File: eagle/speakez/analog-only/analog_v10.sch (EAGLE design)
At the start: 51 parts, among them U1 +12v, U2 MAX5486

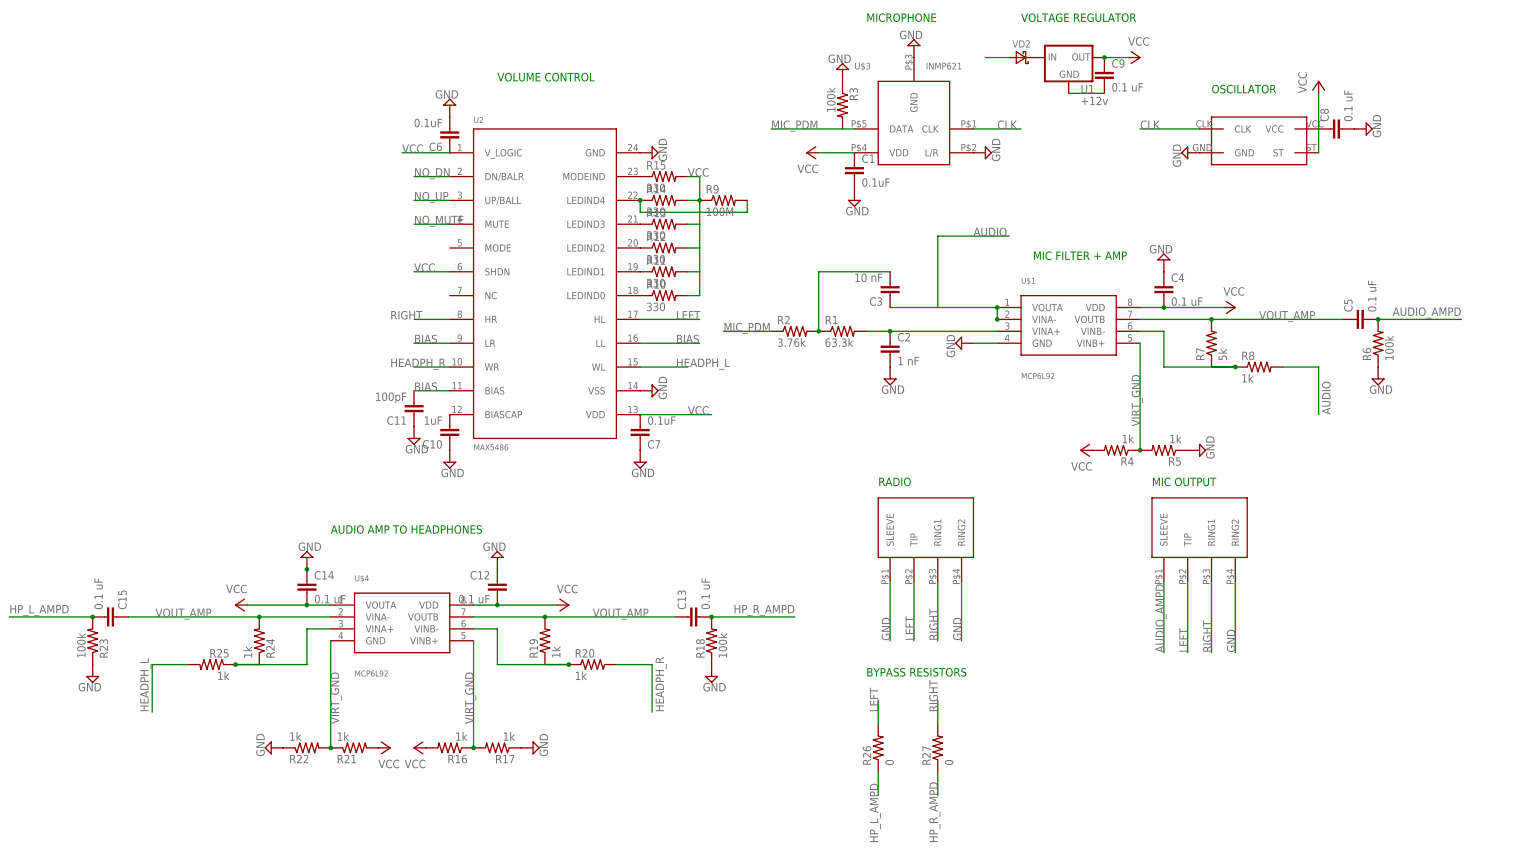
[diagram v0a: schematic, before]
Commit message: update L/R buffering, offsets, naming conventions, move info from nets layer to info layer
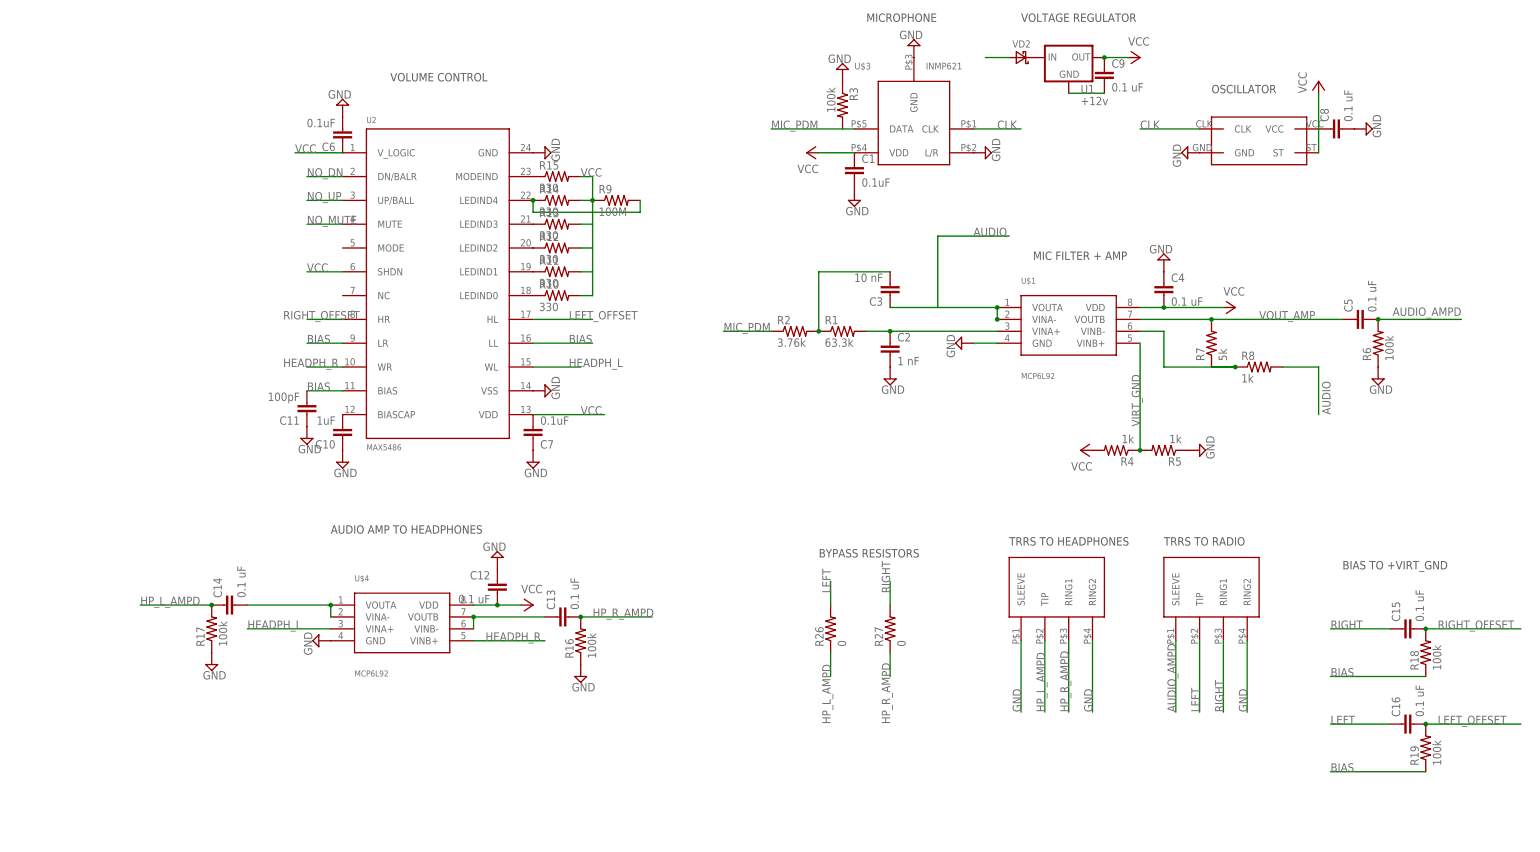
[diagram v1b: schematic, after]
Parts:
- removed R20, R24, R25: 1k, SparkFun-Resistors:RESISTOR0805-RES
- removed R21, R22: 1k, SparkFun-Passives:RESISTOR0805-RES
- removed R23: 100k, SparkFun-Resistors:RESISTOR0805-RES
- added C16: 0.1 uF, SparkFun-Passives:CAP0805
- R16, R17: value 1k -> 100k; device SparkFun-Passives:RESISTOR0805-RES -> SparkFun-Resistors:RESISTOR0805-RES
- R19: value 1k -> 100k
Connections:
- new net LEFT_OFFSET: C16.2, R19.2, U2.HL
- new net RIGHT_OFFSET: C15.2, R18.2, U2.HR
- net BIAS: now also R18.1, R19.1
- net GND: now also R16.1, U$4.GND; no longer C14.1, R18.1, R22.1, R23.1
- net HEADPH_L: now also U$4.VINA+; no longer R25.2
- net HEADPH_R: now also U$4.VINB+; no longer R20.2
- net HP_L_AMPD: now also C14.1, HP.TIP, R17.2; no longer C15.2, R23.2
- net HP_R_AMPD: now also HP.RING1, R16.2; no longer R18.2
- net LEFT: now also C16.1; no longer HP.TIP, U2.HL
- net N$10: now also C13.1, U$4.VOUTB; no longer R19.1, R20.1
- net N$14: now also C14.2, U$4.VINA-, U$4.VOUTA; no longer R24.1, R25.1, U$4.VINA+
- net RIGHT: now also C15.1; no longer HP.RING1, U2.HR
- net VCC: no longer C14.2, R16.2, R21.2, U$4.VOUTA
- net VIRT_GND: no longer R16.1, R17.2, R21.1, R22.2, U$4.GND, U$4.VINB+
- net VOUT_AMP: no longer C13.1, C15.1, R19.2, R24.2, U$4.VINA-, U$4.VOUTB
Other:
- note added: "BIAS TO +VIRT_GND"
- note added: "TRRS TO HEADPHONES"
- note added: "TRRS TO RADIO"
- note removed: "MIC OUTPUT"
- note removed: "RADIO"
- moved on the sheet: C10, C11, C13, C14, C15, C6, C7, R10, R11, R12, R13, R14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

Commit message: routed some of board
but doubting my routing
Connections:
- net GND renamed HEADPHONES_R
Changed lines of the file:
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@@
 <?xml version="1.0" encoding="utf-8"?>
 <!DOCTYPE eagle SYSTEM "eagle.dtd">
-<eagle version="7.6.0">
+<eagle version="7.7.0">
 <drawing>
 <settings>
@@
 <grid distance="0.1" unitdist="inch" unit="inch" style="lines" multiple="1" display="no" altdistance="0.01" altunitdist="inch" altunit="inch"/>
 <layers>
-<layer number="1" name="Top" color="4" fill="1" visible="no" active="no"/>
-<layer number="16" name="Bottom" color="1" fill="1" visible="no" active="no"/>
-<layer number="17" name="Pads" color="2" fill="1" visible="no" active="no"/>
-<layer number="18" name="Vias" color="2" fill="1" visible="no" active="no"/>
-<layer number="19" name="Unrouted" color="6" fill="1" visible="no" active="no"/>
-<layer number="20" name="Dimension" color="15" fill="1" visible="no" active="no"/>
-<layer number="21" name="tPlace" color="8" fill="1" visible="no" active="no"/>
-<layer number="22" name="bPlace" color="7" fill="1" visible="no" active="no"/>
-<layer number="23" name="tOrigins" color="15" fill="1" visible="no" active="no"/>
-<layer number="24" name="bOrigins" color="15" fill="1" visible="no" active="no"/>
-<layer number="25" name="tNames" color="8" fill="1" visible="no" active="no"/>
-<layer number="26" name="bNames" color="7" fill="1" visible="no" active="no"/>
-<layer number="27" name="tValues" color="8" fill="1" visible="no" active="no"/>
-<layer number="28" name="bValues" color="7" fill="1" visible="no" active="no"/>
+<layer number="1" name="Top" color="4" fill="1" visible="yes" active="no"/>
+<layer number="16" name="Bottom" color="1" fill="1" visible="yes" active="no"/>
+<layer number="17" name="Pads" color="2" fill="1" visible="yes" active="no"/>
+<layer number="18" name="Vias" color="2" fill="1" visible="yes" active="no"/>
+<layer number="19" name="Unrouted" color="6" fill="1" visible="yes" active="no"/>
+<layer number="20" name="Dimension" color="15" fill="1" visible="yes" active="no"/>
+<layer number="21" name="tPlace" color="8" fill="1" visible="yes" active="no"/>
+<layer number="22" name="bPlace" color="7" fill="1" visible="yes" active="no"/>
+<layer number="23" name="tOrigins" color="15" fill="1" visible="yes" active="no"/>
+<layer number="24" name="bOrigins" color="15" fill="1" visible="yes" active="no"/>
+<layer number="25" name="tNames" color="8" fill="1" visible="yes" active="no"/>
+<layer number="26" name="bNames" color="7" fill="1" visible="yes" active="no"/>
+<layer number="27" name="tValues" color="8" fill="1" visible="yes" active="no"/>
+<layer number="28" name="bValues" color="7" fill="1" visible="yes" active="no"/>
 <layer number="29" name="tStop" color="7" fill="3" visible="no" active="no"/>
 <layer number="30" name="bStop" color="7" fill="6" visible="no" active="no"/>
@@
 <layer number="35" name="tGlue" color="7" fill="4" visible="no" active="no"/>
 <layer number="36" name="bGlue" color="7" fill="5" visible="no" active="no"/>
-<layer number="37" name="tTest" color="7" fill="1" visible="no" active="no"/>
-<layer number="38" name="bTest" color="7" fill="1" visible="no" active="no"/>
+<layer number="37" name="tTest" color="7" fill="1" visible="yes" active="no"/>
+<layer number="38" name="bTest" color="7" fill="1" visible="yes" active="no"/>
 <layer number="39" name="tKeepout" color="4" fill="11" visible="no" active="no"/>
 <layer number="40" name="bKeepout" color="1" fill="11" visible="no" active="no"/>
@@
 <layer number="44" name="Drills" color="7" fill="1" visible="no" active="no"/>
 <layer number="45" name="Holes" color="7" fill="1" visible="no" active="no"/>
-<layer number="46" name="Milling" color="3" fill="1" visible="no" active="no"/>
-<layer number="47" name="Measures" color="7" fill="1" visible="no" active="no"/>
-<layer number="48" name="Document" color="7" fill="1" visible="no" active="no"/>
-<layer number="49" name="Reference" color="7" fill="1" visible="no" active="no"/>
-<layer number="50" name="dxf" color="7" fill="1" visible="no" active="no"/>
-<layer number="51" name="tDocu" color="7" fill="1" visible="no" active="no"/>
-<layer number="52" name="bDocu" color="7" fill="1" visible="no" active="no"/>
-<layer number="53" name="tGND_GNDA" color="7" fill="9" visible="no" active="no"/>
-<layer number="54" name="bGND_GNDA" color="1" fill="9" visible="no" active="no"/>
-<layer number="56" name="wert" color="7" fill="1" visible="no" active="no"/>
-<layer number="57" name="tCAD" color="7" fill="1" visible="no" active="no"/>
-<layer number="59" name="tCarbon" color="7" fill="1" visible="no" active="no"/>
-<layer number="60" name="bCarbon" color="7" fill="1" visible="no" active="no"/>
+<layer number="46" name="Milling" color="3" fill="1" visible="yes" active="no"/>
+<layer number="47" name="Measures" color="7" fill="1" visible="yes" active="no"/>
+<layer number="48" name="Document" color="7" fill="1" visible="yes" active="no"/>
+<layer number="49" name="Reference" color="7" fill="1" visible="yes" active="no"/>
+<layer number="50" name="dxf" color="7" fill="1" visible="yes" active="no"/>
+<layer number="51" name="tDocu" color="7" fill="1" visible="yes" active="no"/>
+<layer number="52" name="bDocu" color="7" fill="1" visible="yes" active="no"/>
+<layer number="53" name="tGND_GNDA" color="7" fill="9" visible="yes" active="no"/>
+<layer number="54" name="bGND_GNDA" color="1" fill="9" visible="yes" active="no"/>
+<layer number="56" name="wert" color="7" fill="1" visible="yes" active="no"/>
+<layer number="57" name="tCAD" color="7" fill="1" visible="yes" active="no"/>
+<layer number="59" name="tCarbon" color="7" fill="1" visible="yes" active="no"/>
+<layer number="60" name="bCarbon" color="7" fill="1" visible="yes" active="no"/>
 <layer number="90" name="Modules" color="5" fill="1" visible="yes" active="yes"/>
 <layer number="91" name="Nets" color="2" fill="1" visible="yes" active="yes"/>
@@
 </busses>
 <nets>
-<net name="GND" class="0">
+<net name="HEADPHONES_R" class="0">
 <segment>
 <pinref part="U$1" gate="G$1" pin="GND"/>

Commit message: did some more layout, fixed some random things
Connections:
- net HEADPHONES_R renamed GND
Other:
- moved on the sheet: VD2

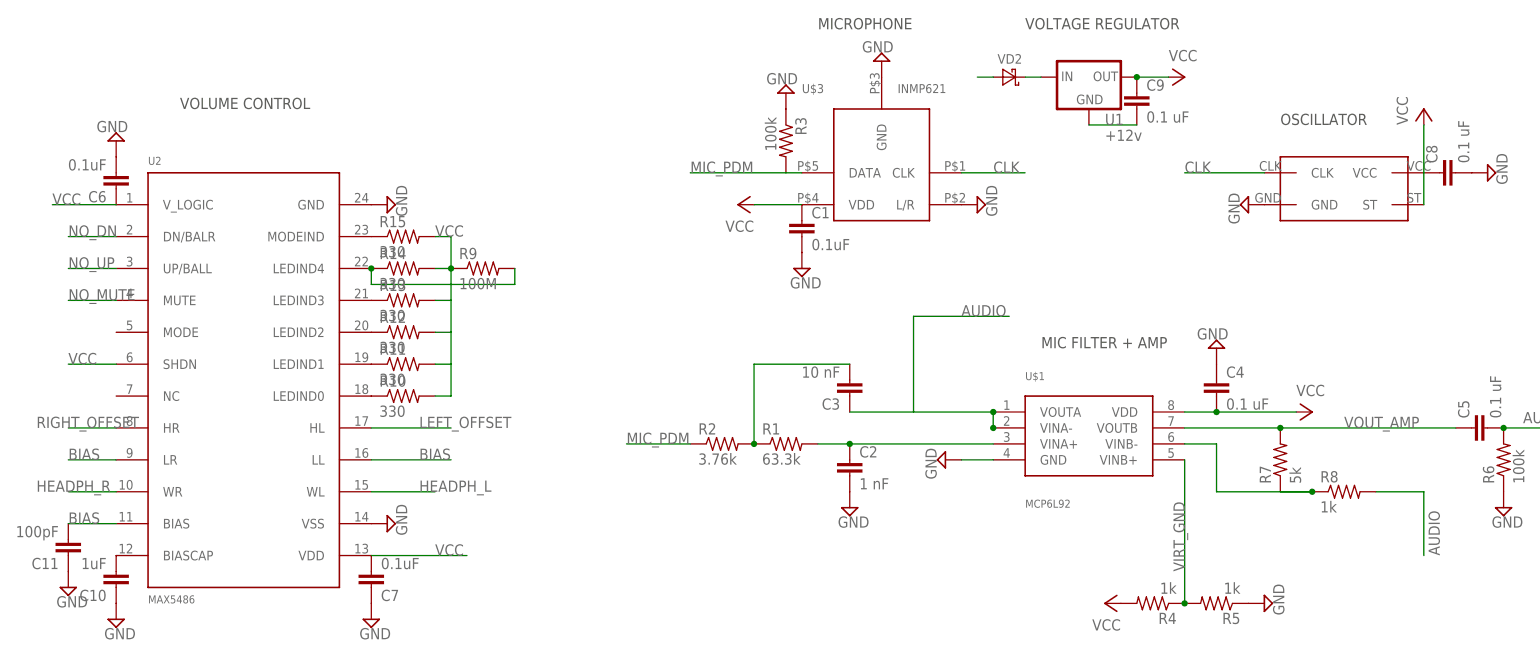
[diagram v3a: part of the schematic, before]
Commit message: tweaking things, clearing out some clearance errors
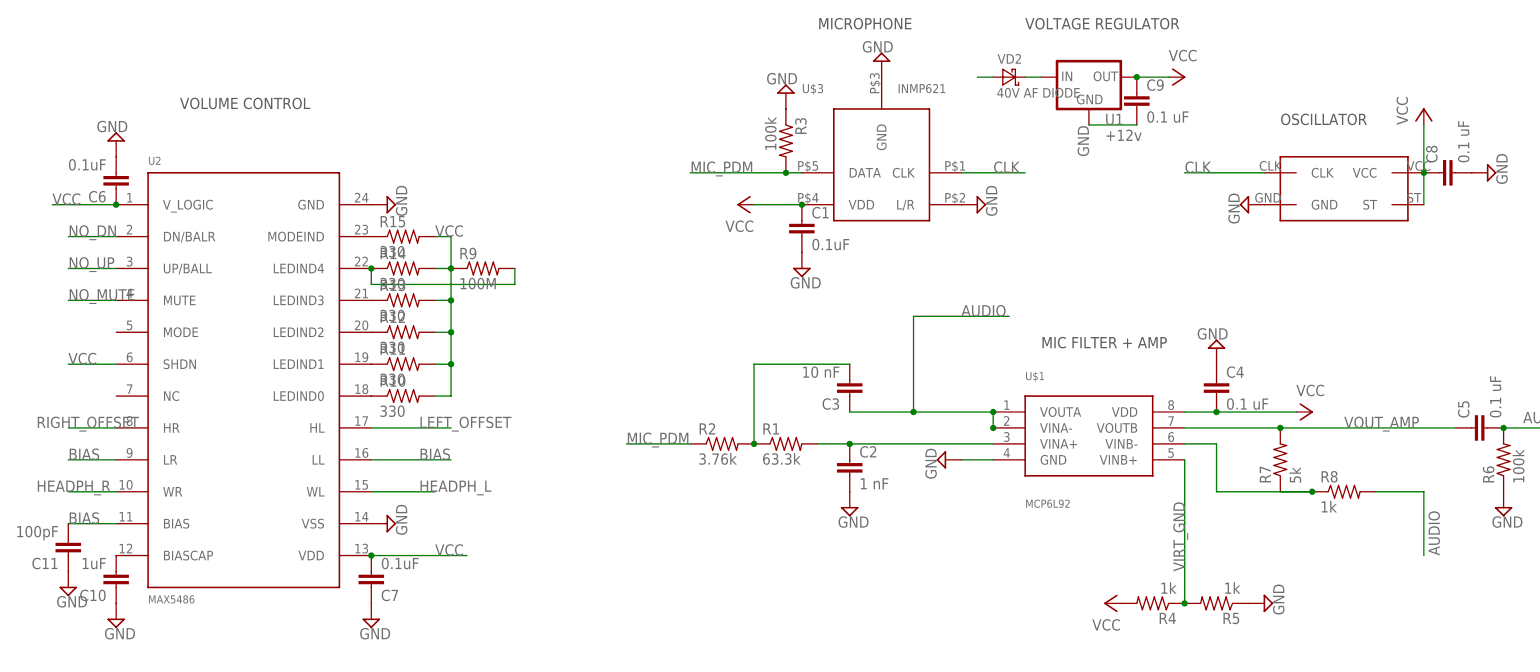
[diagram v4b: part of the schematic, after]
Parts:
- VD2: value (none) -> 40V AF DIODE
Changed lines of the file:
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@@
 <part name="HP" library="35mm_audio" deviceset="SJ-43514-SMT" device=""/>
 <part name="RADIO" library="35mm_audio" deviceset="SJ-43514-SMT" device=""/>
-<part name="VD2" library="diode" deviceset="DIODE-SCHOTTKY-" device="SOD123"/>
+<part name="VD2" library="diode" deviceset="DIODE-SCHOTTKY-" device="SOD123" value="40V AF DIODE"/>
 <part name="U2" library="MAX5486" deviceset="MAX5486" device=""/>
 <part name="SUPPLY10" library="supply2" deviceset="GND" device=""/>
@@
 <pinref part="U$2" gate="G$1" pin="ST"/>
 <wire x1="116.84" y1="99.06" x2="116.84" y2="104.14" width="0.1524" layer="91"/>
+<junction x="116.84" y="104.14"/>
 </segment>
 <segment>
@@
 <pinref part="P+4" gate="VCC" pin="VCC"/>
 <wire x1="17.78" y1="99.06" x2="10.16" y2="99.06" width="0.1524" layer="91"/>
+<junction x="17.78" y="99.06"/>
 </segment>
 <segment>
@@
 <wire x1="-101.6" y1="99.06" x2="-91.44" y2="99.06" width="0.1524" layer="91"/>
 <label x="-101.6" y="99.06" size="1.778" layer="95"/>
+<junction x="-91.44" y="99.06"/>
 </segment>
 <segment>
@@
 <wire x1="-50.8" y1="43.18" x2="-35.56" y2="43.18" width="0.1524" layer="91"/>
 <label x="-40.64" y="43.18" size="1.778" layer="95"/>
+<junction x="-50.8" y="43.18"/>
 </segment>
 <segment>
@@
 <pinref part="R14" gate="G$1" pin="2"/>
 <pinref part="R15" gate="G$1" pin="2"/>
+<junction x="-38.1" y="73.66"/>
+<junction x="-38.1" y="78.74"/>
+<junction x="-38.1" y="83.82"/>
 </segment>
 <segment>
@@
 <wire x1="15.24" y1="104.14" x2="0" y2="104.14" width="0.1524" layer="91"/>
 <label x="0" y="104.14" size="1.778" layer="95"/>
+<junction x="15.24" y="104.14"/>
 </segment>
 </net>
@@
 <junction x="48.26" y="63.5"/>
 <wire x1="35.56" y1="81.28" x2="35.56" y2="66.04" width="0.1524" layer="91"/>
+<junction x="35.56" y="66.04"/>
 </segment>
 </net>
@@
 <pinref part="U1" gate="G$1" pin="GND"/>
 <wire x1="71.12" y1="111.76" x2="63.5" y2="111.76" width="0.1524" layer="91"/>
+<label x="63.5" y="106.68" size="1.778" layer="95" rot="R90"/>
 </segment>
 <segment>
@@
 </sheet>
 </sheets>
+<errors>
+</errors>
 </schematic>
 </drawing>
